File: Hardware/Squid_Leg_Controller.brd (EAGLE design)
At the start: 29.5 x 27.3 mm, 11 parts, among them IC1 REG1117, J1 SPI_PRG, Q1 MMBT2222A

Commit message: saving progress on adding in buzzer and led controls
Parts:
- removed JP1: (no value), SparkFun-Connectors:1X07_LOCK
- removed U$3: NRF24L01+_MODULE, Dan9186 - RF:NRF24L01+_MODULE
- added JP3: (no value), SparkFun-Connectors:1X06_LOCK
- added Q2: MOSFET-NCHANNEL_DUALFDMA1024NZ, SparkFun-DiscreteSemi:MICROFET_2X2
- added R2, R3: 100, resistor:M0805
- added U$4: NRF24L01+, Derp - RF:NRF24L01+_MODULE_OFFBRD
- moved C2 12.0 mm to (11.3, 22.4), turned to 0 degrees
- moved C1 8.90 mm to (11.9, 26.0)
- moved IC1 4.83 mm to (10.4, 16.3)
- moved U$2 2.01 mm to (4.45, 24.1)
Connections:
- removed net N$3: JP1.3
- removed net N$4: JP1.4
- removed net N$6: JP1.5
- removed net N$7: JP1.6
- removed net N$8: JP1.7
- new net BUZZ: JP3.3
- new net BUZZ_CTL: Q2.G2, U$1.6
- new net LED: JP3.4
- new net LED_CTL: Q2.G1, U$1.3
- new net N$1: Q2.D1_2, R2.2
- new net N$2: Q2.D2_2, R3.2
- new net WD0: JP3.5, U$1.11
- new net WD1: JP3.6, U$1.10
- net 12V: now also JP3.1; no longer JP1.1
- net 3.3V: now also U$4.3.3V; no longer U$3.3.3V
- net CE: now also U$4.CE; no longer U$3.CE
- net CSN: now also U$4.CSN; no longer U$3.CSN
- net GND: now also JP3.2, Q2.S1, Q2.S2, U$4.GND; no longer JP1.2, U$3.GND
- net IRQ: now also U$4.IRQ; no longer U$3.IRQ
- net MISO: now also U$4.MISO; no longer U$3.MISO
- net MOSI: now also U$4.MOSI; no longer U$3.MOSI
- net SCK: now also U$4.SCK; no longer U$3.SCK
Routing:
- net GND: track 54.4 -> 26.8 mm
- net 12V: track 45.3 -> 20.1 mm
- net WD0: track 0.00 -> 15.4 mm
- net SCK: track 29.2 -> 18.1 mm
- net RESET: track 10.3 -> 0.00 mm
- net RELAY_CTL: track 9.17 -> 0.00 mm
- net WD1: track 0.00 -> 8.66 mm
- net MOSI: track 39.1 -> 40.6 mm
- net 3.3V: track 53.5 -> 54.5 mm
- net MISO: track 21.6 -> 22.1 mm
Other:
- board size 29.5 x 27.3 mm -> 30.1 x 28.6 mm

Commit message: routed remainig pieces, added in mosfet to control LED and buzzer, and attached DRU
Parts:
- R1, R2, R3: device resistor:M0805 -> resistor:R0805
- moved R2 40.2 mm to (12.7, 4.83), turned to 90 degrees
- moved R3 38.8 mm to (10.3, 4.83), turned to 90 degrees
- moved Q2 9.80 mm to (15.0, 8.38), turned to 90 degrees
- moved Q1 5.43 mm to (6.99, 5.71)
- moved R1 1.91 mm to (6.35, 2.54), turned to 0 degrees
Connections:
- net BUZZ: now also R3.1
- net BUZZ_CTL: now also U$1.3; no longer U$1.6
- net LED: now also R2.1
- net LED_CTL: now also U$1.2; no longer U$1.3
- net N$5: now also R1.2; no longer R1.1
- net RELAY: now also R1.1; no longer R1.2
- net RELAY_CTL: now also U$1.6; no longer U$1.2
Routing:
- net RELAY_CTL: track 0.00 -> 41.5 mm, vias 0 -> 2
- net GND: track 26.8 -> 0.37 mm
- net LED: track 0.00 -> 23.7 mm
- net BUZZ: track 0.00 -> 23.4 mm, vias 0 -> 1
- net N$1: track 0.00 -> 8.76 mm, vias 0 -> 2
- net LED_CTL: track 0.00 -> 7.56 mm
- net RESET: track 0.00 -> 6.88 mm
- net N$2: track 0.00 -> 6.56 mm
- net BUZZ_CTL: track 0.00 -> 5.00 mm
- net RELAY: track 4.64 -> 2.83 mm
- net N$5: track 2.89 -> 2.29 mm
- added copper zone on layer 16, net 12V
- removed copper zone on layer 16, net GND

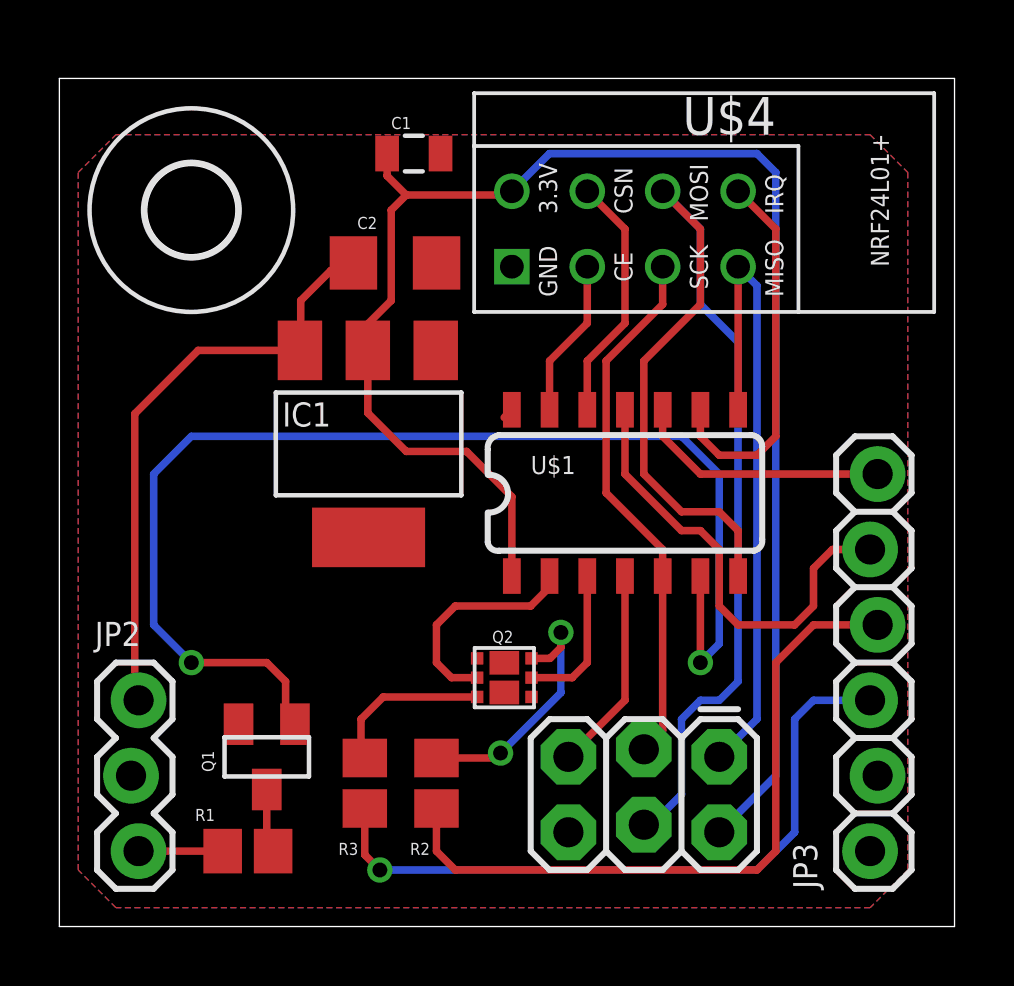
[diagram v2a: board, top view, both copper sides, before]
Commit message: updated missing resistors and removed traces on board, tracing needs to be redone
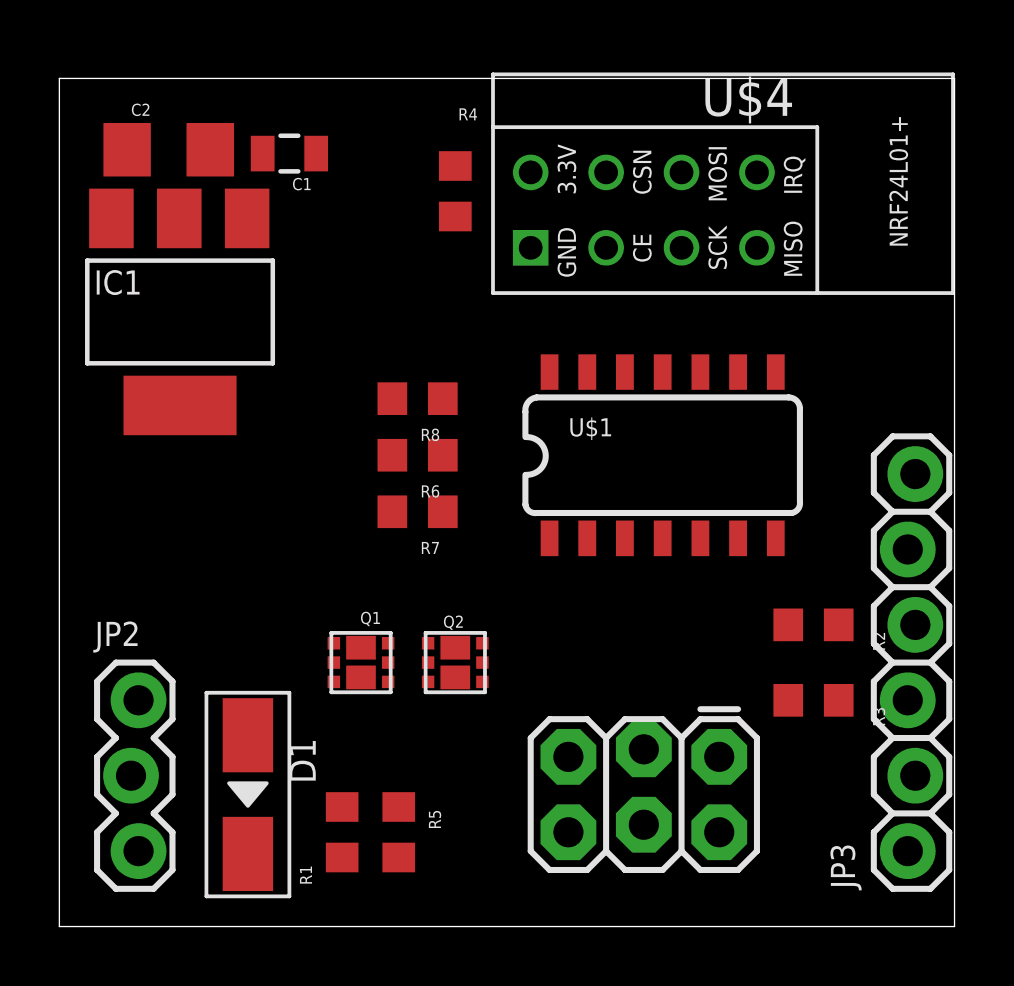
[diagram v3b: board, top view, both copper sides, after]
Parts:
- removed U$2: (no value), holes:3,0
- added D1: (no value), OPL Eagle Library:DO-214AC
- added R4, R5: 10K, resistor:R0603
- added R6, R7, R8: 1K, resistor:R0603
- Q1: value MMBT2222A -> MOSFET-NCHANNEL_DUALFDMA1024NZ; device SparkFun-DiscreteSemi:SOT23 -> SparkFun-DiscreteSemi:MICROFET_2X2
- R1, R2, R3: device resistor:R0805 -> resistor:R0603
- moved R3 15.4 mm to (25.4, 7.62), turned to 180 degrees
- moved R2 13.8 mm to (25.4, 10.2), turned to 180 degrees
- moved C2 8.52 mm to (3.68, 26.2)
- moved IC1 7.75 mm to (4.06, 20.7)
- moved Q1 4.49 mm to (10.2, 8.89), turned to 270 degrees
- moved C1 4.19 mm to (7.75, 26.0), turned to 180 degrees
- moved R1 3.24 mm to (9.53, 3.17), turned to 90 degrees
- moved U$1 1.80 mm to (20.3, 15.9)
- moved Q2 1.73 mm to (13.3, 8.89)
- moved JP3 1.27 mm to (28.6, 2.54)
- moved U$4 0.90 mm to (22.2, 35.6)
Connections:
- net 12V renamed VCC
- new net N$3: R6.1, U$1.3
- new net N$4: R7.1, U$1.2
- new net N$8: R8.1, U$1.6
- net 3.3V: now also R4.2, R5.2
- net BUZZ_CTL: now also R6.2; no longer U$1.3
- net CE: now also R4.1
- net GND: now also D1.1, Q1.S1; no longer Q1.2
- net LED_CTL: now also R7.2; no longer U$1.2
- net N$5: now also Q1.D1_2; no longer Q1.3
- net RELAY: now also D1.2
- net RELAY_CTL: now also Q1.G1, R8.2; no longer Q1.1, U$1.6
- net RESET: now also R5.1
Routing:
- net 3.3V: track 54.5 -> 0.00 mm
- net RELAY_CTL: track 41.5 -> 0.00 mm, vias 2 -> 0
- net MOSI: track 40.6 -> 0.00 mm
- net LED: track 23.7 -> 0.00 mm
- net BUZZ: track 23.4 -> 0.00 mm, vias 1 -> 0
- net MISO: track 22.1 -> 0.00 mm
- net VCC: track 20.1 -> 0.00 mm
- net SCK: track 18.1 -> 0.00 mm
- net WD0: track 15.4 -> 0.00 mm
- net IRQ: track 12.7 -> 0.00 mm
- net N$1: track 8.76 -> 0.00 mm, vias 2 -> 0
- net WD1: track 8.66 -> 0.00 mm
- net CSN: track 8.41 -> 0.00 mm
- net LED_CTL: track 7.56 -> 0.00 mm
- net RESET: track 6.88 -> 0.00 mm
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- removed copper zone on layer 1, net GND
- removed copper zone on layer 16, net VCC

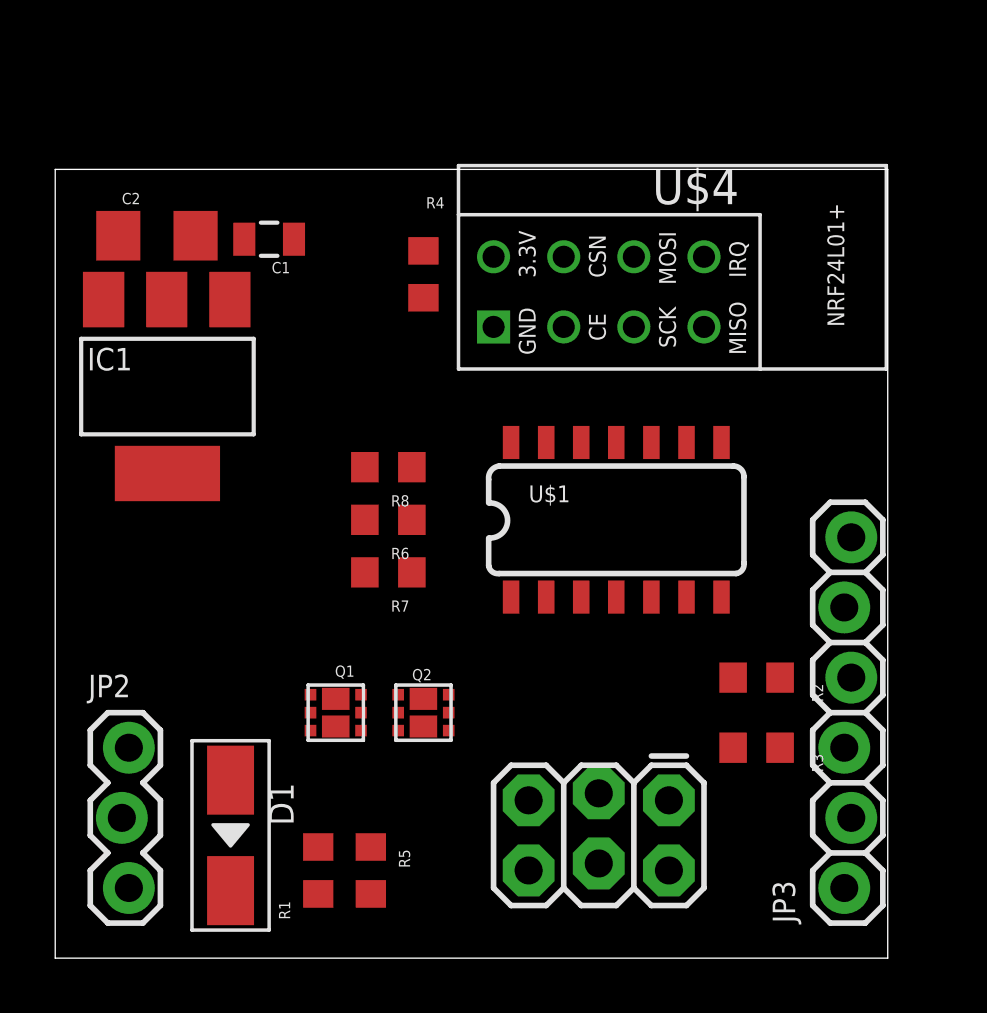
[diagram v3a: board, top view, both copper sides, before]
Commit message: added button and rerouted board
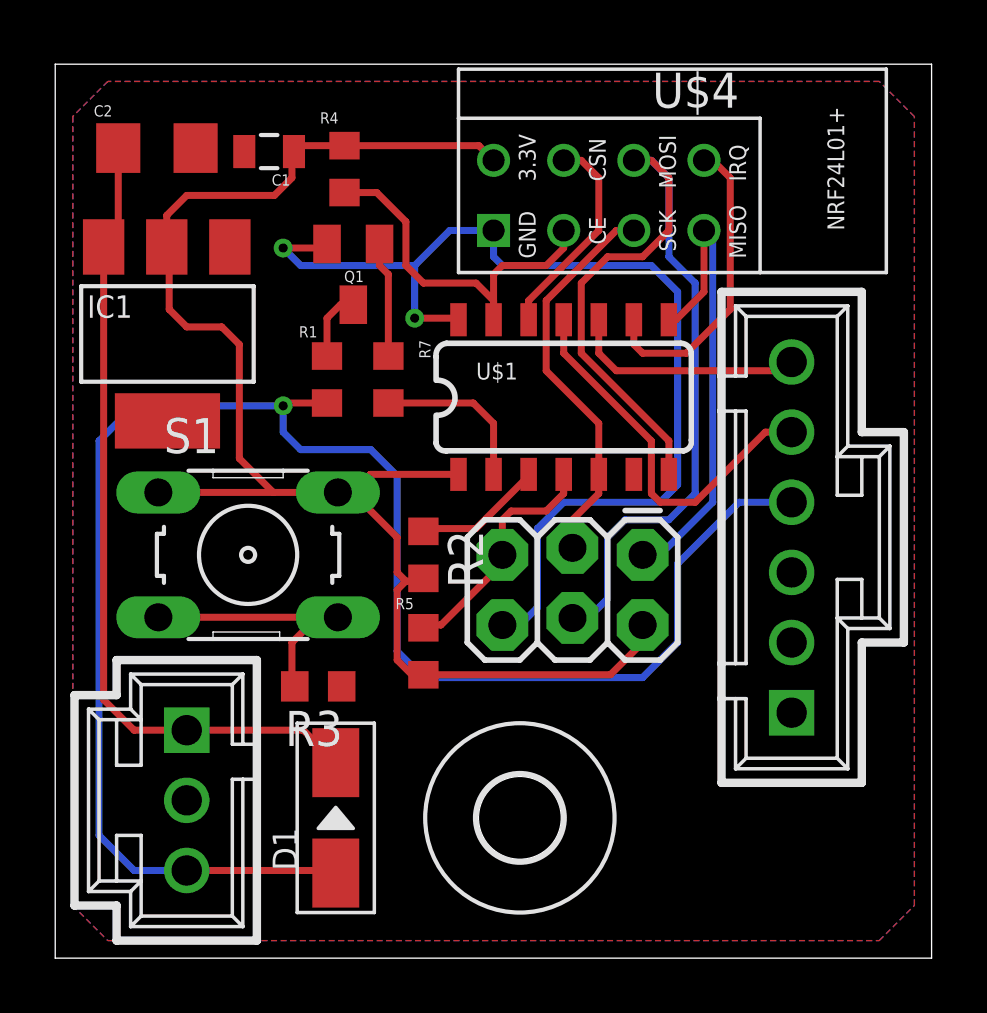
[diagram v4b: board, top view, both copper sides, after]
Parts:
- removed JP2: (no value), SparkFun-Connectors:1X03_LOCK
- removed JP3: (no value), SparkFun-Connectors:1X06_LOCK
- removed Q2: MOSFET-NCHANNEL_DUALFDMA1024NZ, SparkFun-DiscreteSemi:MICROFET_2X2
- removed R6, R8: 1K, resistor:R0603
- added S1: (no value), switch-omron:B3F-10XX
- added U$2: (no value), holes:3,0
- added X1: HEADER_POS3_70543, Derp - Connectors - Molex SL:70543-POS3
- added X2: HEADER_POS6_70543, Derp - Connectors - Molex SL:70543-POS6
- Q1: value MOSFET-NCHANNEL_DUALFDMA1024NZ -> (none); device SparkFun-DiscreteSemi:MICROFET_2X2 -> adafruit:SOT23
- R2: value 100 -> 1K
- R3: value 100 -> 10K
- moved R1 17.8 mm to (9.84, 21.0)
- moved R3 16.0 mm to (9.53, 9.84)
- moved Q1 15.9 mm to (10.8, 24.8), turned to 180 degrees
- moved R2 12.9 mm to (13.3, 14.6), turned to 270 degrees
- moved J1 8.94 mm to (21.3, 14.6)
- moved R5 8.16 mm to (13.3, 11.1)
- moved R7 6.98 mm to (12.1, 21.0), turned to 90 degrees
- moved U$1 4.84 mm to (18.4, 20.3)
- moved R4 4.76 mm to (10.5, 28.6)
- moved D1 3.86 mm to (10.2, 5.08), turned to 90 degrees
- moved U$4 3.49 mm to (22.2, 39.1)
- moved C1 3.18 mm to (7.75, 29.2)
- moved C2 3.18 mm to (3.68, 29.3)
- moved IC1 1.91 mm to (4.06, 22.6)
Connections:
- removed net BUZZ_CTL: Q2.G2, R6.2
- removed net LED: JP3.4, R2.1
- removed net LED_CTL: Q2.G1, R7.2
- removed net N$3: R6.1, U$1.3
- removed net N$8: R8.1, U$1.6
- removed net RELAY: D1.2, JP2.3, R1.1
- new net RELAY_LED: D1.1, R1.1, X1.P$3, X2.P$4
- net 3.3V: now also R2.2, S1.1, S1.2
- net BUZZ: now also X2.P$3; no longer JP3.3, R3.1
- net GND: now also Q1.2, R3.1, X1.P$2, X2.P$2; no longer D1.1, JP2.2, JP3.2, Q1.S1, Q2.S1, Q2.S2
- net N$1: now also R2.1, U$1.3; no longer Q2.D1_2, R2.2
- net N$2: now also S1.3, S1.4; no longer Q2.D2_2
- net N$5: now also Q1.3; no longer Q1.D1_2
- net RELAY_CTL: now also Q1.1, R7.2; no longer Q1.G1, R8.2
- net VCC: now also D1.2, X1.P$1, X2.P$1; no longer JP2.1, JP3.1
- net WD0: now also X2.P$5; no longer JP3.5
- net WD1: now also X2.P$6; no longer JP3.6
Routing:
- net RELAY_LED: track 0.00 -> 63.3 mm, vias 0 -> 1
- net 3.3V: track 0.00 -> 55.0 mm
- net GND: track 0.00 -> 39.1 mm, vias 0 -> 2
- net MOSI: track 0.00 -> 36.6 mm
- net VCC: track 0.00 -> 29.5 mm
- net MISO: track 0.00 -> 17.2 mm
- net SCK: track 0.00 -> 14.4 mm
- net WD0: track 0.00 -> 13.9 mm
- net CE: track 0.00 -> 13.9 mm
- net IRQ: track 0.00 -> 11.2 mm
- net N$2: track 0.00 -> 9.43 mm
- net RESET: track 0.00 -> 8.72 mm
- net WD1: track 0.00 -> 8.59 mm
- net CSN: track 0.00 -> 7.72 mm
- net N$4: track 0.00 -> 5.96 mm
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- added copper zone on layer 1, net GND
- added copper zone on layer 16, net VCC
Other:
- board size 30.1 x 28.6 mm -> 31.7 x 32.4 mm

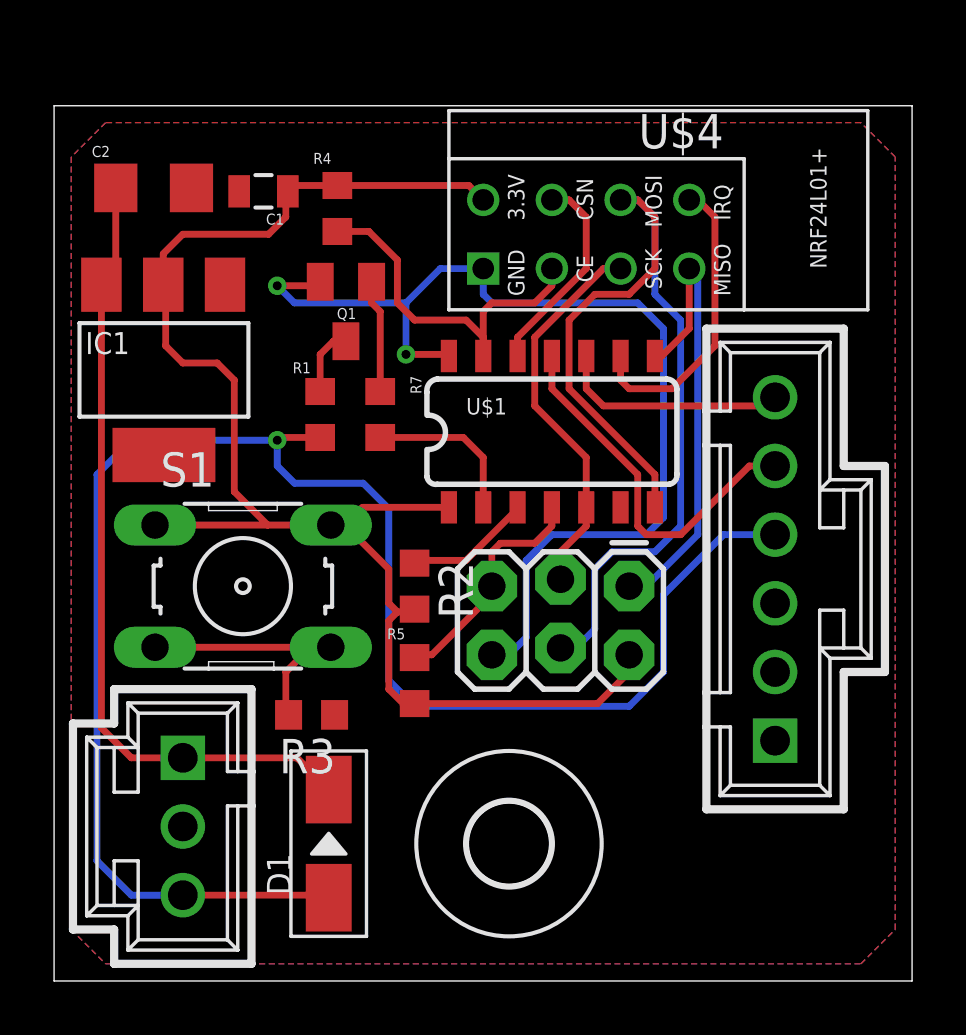
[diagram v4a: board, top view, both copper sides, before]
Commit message: slight adjustment to board, better silk screen, changed switch to locking connector, broke out extra IO, and moved mounting hole
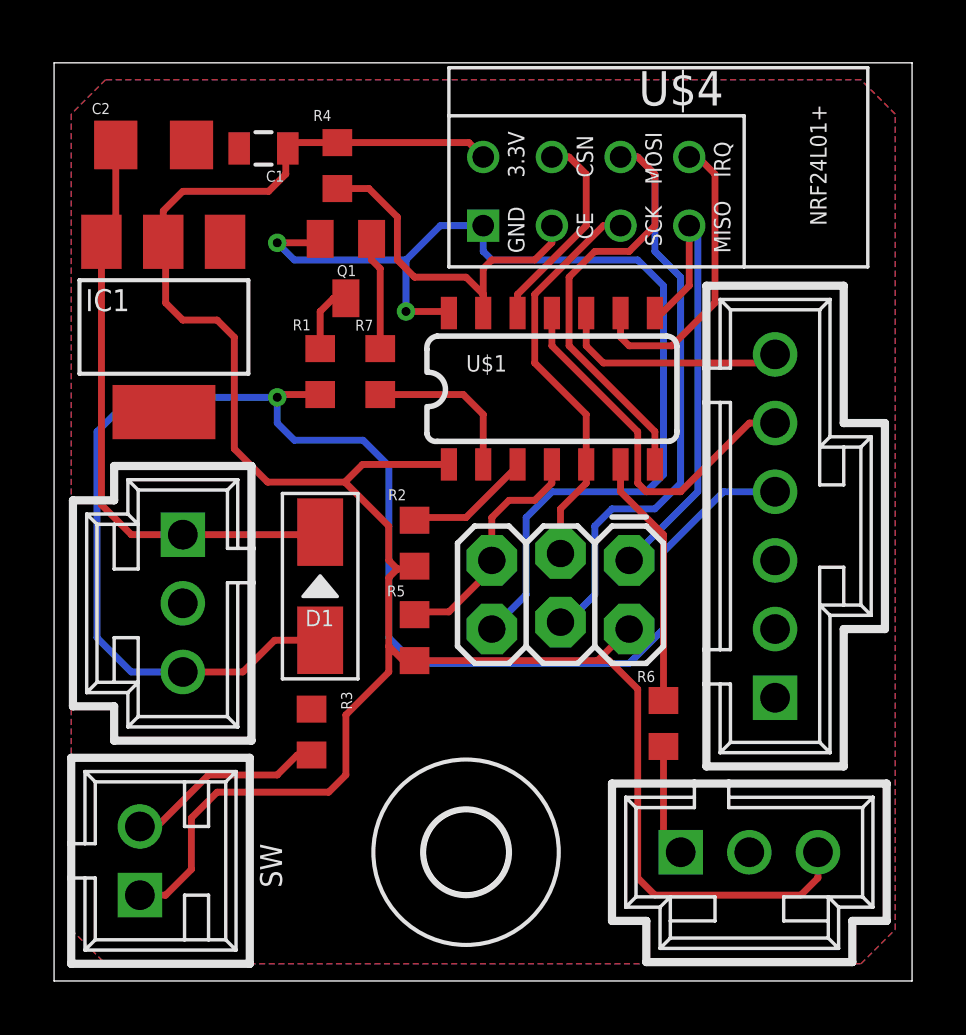
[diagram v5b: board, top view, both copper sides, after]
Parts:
- removed S1: (no value), switch-omron:B3F-10XX
- added R6: 1K, resistor:R0603
- added X3: SW, Derp - Connectors - Molex SL:70543-POS2
- added X4: XTRA, Derp - Connectors - Molex SL:70543-POS3
- moved D1 9.53 mm to (9.84, 14.6)
- moved X1 8.26 mm to (4.76, 14.0)
- moved U$2 1.62 mm to (15.2, 4.76)
- moved R1 1.59 mm to (9.84, 22.5)
- moved R4 1.59 mm to (10.5, 30.2)
- moved R7 1.59 mm to (12.1, 22.5)
- moved X2 1.59 mm to (26.7, 16.8)
- moved C1 1.59 mm to (7.75, 30.8)
- moved C2 1.59 mm to (3.68, 30.9)
- moved IC1 1.59 mm to (4.06, 24.2)
- moved Q1 1.59 mm to (10.8, 26.4)
- moved R2 1.59 mm to (13.3, 16.2)
- moved R5 1.59 mm to (13.3, 12.7)
- moved U$1 1.59 mm to (18.4, 21.9)
- moved U$4 1.59 mm to (22.2, 40.6)
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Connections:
- new net N$3: R6.1, U$1.6
- new net N$6: R6.2, X4.P$1
- net 3.3V: now also X3.P$1, X4.P$3; no longer S1.1, S1.2
- net GND: now also X4.P$2
- net N$2: now also X3.P$2; no longer S1.3, S1.4
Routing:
- net 3.3V: track 55.0 -> 83.3 mm
- net N$3: track 0.00 -> 9.39 mm
- net VCC: track 29.5 -> 22.2 mm
- net RELAY_LED: track 63.3 -> 56.8 mm
- net N$6: track 0.00 -> 4.36 mm
- net N$2: track 9.43 -> 7.44 mm
- net SCK: track 14.4 -> 15.0 mm
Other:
- board size 31.7 x 32.4 mm -> 31.7 x 34 mm
- board text added: "SW"
